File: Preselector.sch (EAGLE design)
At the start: 100 parts, among them IC58 LMZ31707RVQ, Q2 FDV303N, X1 0733660061, X2 0733660061, X3 0733660061, X4 0733660061, X5 0733660061, X6 0733660061

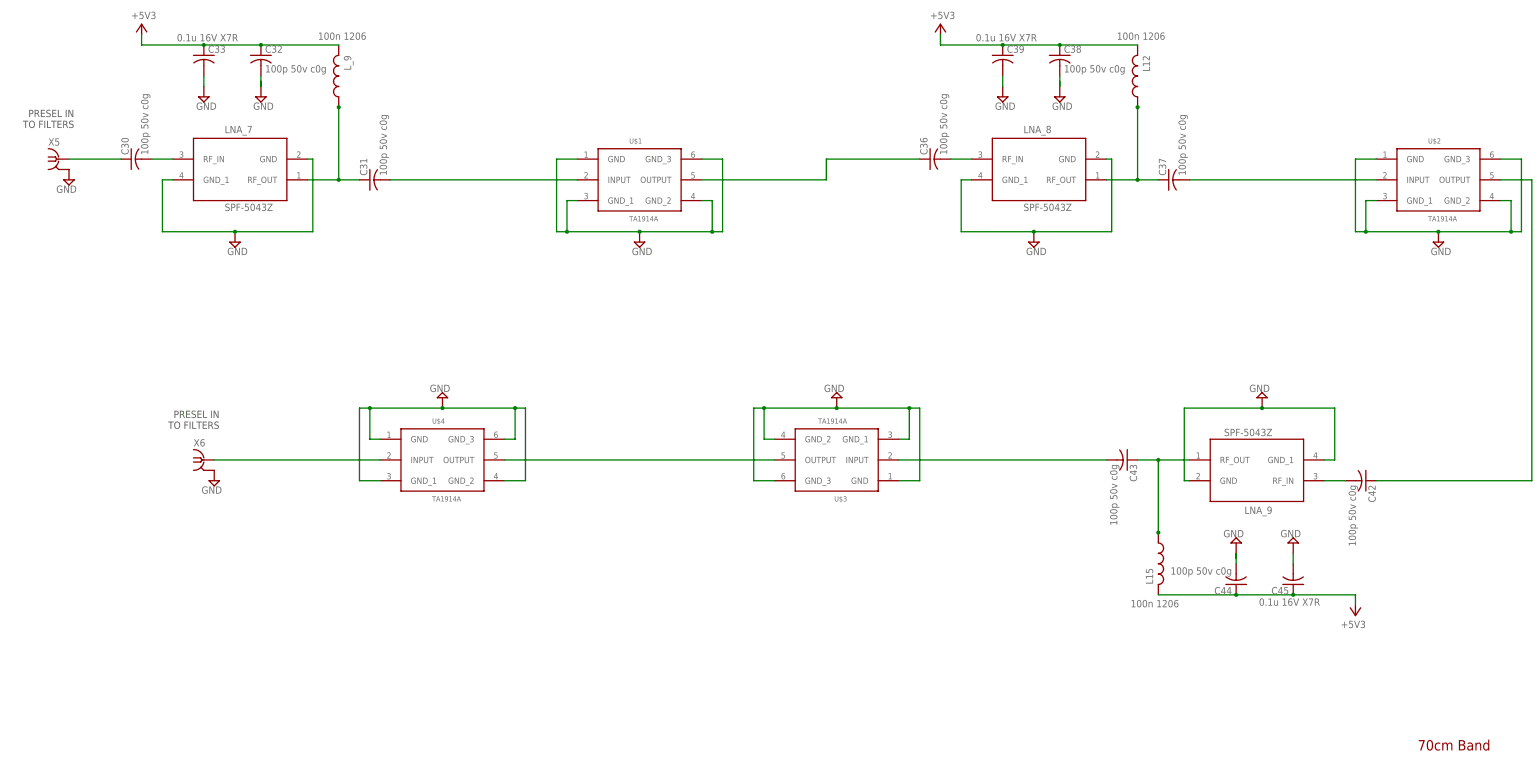
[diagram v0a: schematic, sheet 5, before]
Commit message: Ken, I renamed the capacitors and inductors in order as they appear on each Filter and LNA respectively. If you see anything wrong let me know.
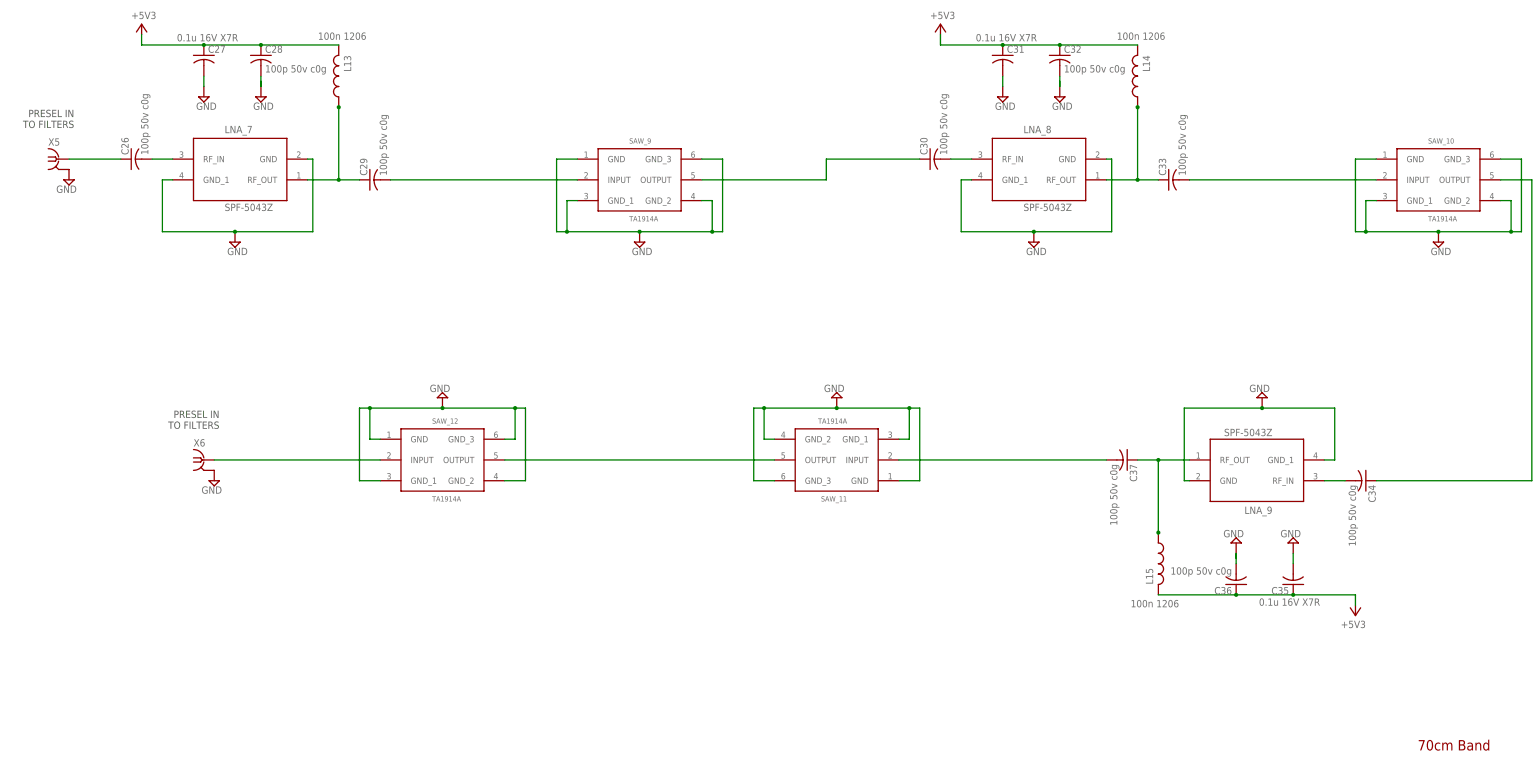
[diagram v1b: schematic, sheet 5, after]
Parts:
- removed C38, C43, C44: 100p 50v c0g, rcl:C-USC0603K
- removed C39: 0.1u 16V X7R, rcl:C-USC0603K
- removed L_8: 100n 1206, NewSDR:L-US1206
- added C14, C17, C20, C21: 100p 50v c0g, rcl:C-USC0603K
- added L14: 100n 1206, NewSDR:L-US1206
- C19, C23, C27, C31: value 100p 50v c0g -> 0.1u 16V X7R
- C25, C29, C33: value 0.1u 16V X7R -> 100p 50v c0g
- renumbered C42 to C34, C45 to C35, C_20 to C16, C_21 to C15, L_00 to L11, L_7 to L10, L_9 to L13, U$1 to SAW_9, U$2 to SAW_10, U$3 to SAW_11, U$4 to SAW_12
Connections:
- net +5V3: now also C19.1, C20.1, C23.1, C27.1, C31.1, C36.1, L14.2; no longer C25.1, C29.1, C33.1, C38.1, C39.1, C44.1, L12.2
- net 1.25M_RF_IN: now also C17.2; no longer C19.2
- net 1.25M_RF_IN1: now also C22.2; no longer C26.2
- net 1.25M_RF_IN3: now also C18.1, C18.2; no longer C22.1, C22.2
- net 1.25M_RF_IN_: now also C21.2; no longer C23.2
- net 1.25M_RF_IN_1: now also C25.2; no longer C27.2
- net 1.2M5_RF_IN4: now also C22.1; no longer C26.1
- net 2M_RF_IN2: now also C14.1, C14.2; no longer C18.1, C18.2
- net 2M_RF_IN4: now also C26.1, C26.2; no longer C30.1, C30.2
- net 2M_RF_IN6: now also C30.2; no longer C36.2
- net GND: now also C19.2, C20.2, C23.2, C27.2, C31.2, C36.2; no longer C25.2, C29.2, C33.2, C38.2, C39.2, C44.2
- net GND1: now also C21.1; no longer C23.1
- net GND2: now also C17.1; no longer C19.1
- net GND3: now also L12.1; no longer L_8.1
- net GND4: now also C29.1; no longer C31.1
- net GND5: now also C33.1, L14.1; no longer C37.1, L12.1
- net GND6: now also C37.1; no longer C43.1
- net N$13: now also C25.1, L12.2; no longer C27.1, L_8.2
- net N$15: now also C29.2; no longer C31.2
- net N$16: now also C30.1; no longer C36.1
- net N$17: now also C33.2; no longer C37.2
- net N$19: now also C37.2; no longer C43.2
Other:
- moved on the sheet: C18, C19, C22, C23, C24, C25, C30, C31, C32, C33, C36, C37

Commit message: Deleted .brd to sync schematic for annotation
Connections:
- removed net N$3: C8.2, L5.2, SAW_3.INPUT
- net 2M_RF_IN: now also C8.2, L5.2, SAW_3.INPUT
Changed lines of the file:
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@@
 <junction x="156.21" y="152.4"/>
+</segment>
+<segment>
+<pinref part="C8" gate="G$1" pin="2"/>
+<pinref part="SAW_3" gate="G$1" pin="INPUT"/>
+<wire x1="322.58" y1="224.79" x2="332.74" y2="224.79" width="0.1524" layer="91"/>
+<pinref part="L5" gate="G$1" pin="2"/>
+<wire x1="332.74" y1="224.79" x2="347.98" y2="224.79" width="0.1524" layer="91"/>
+<wire x1="332.74" y1="224.79" x2="332.74" y2="232.41" width="0.1524" layer="91"/>
+<junction x="332.74" y="224.79"/>
 </segment>
 </net>
@@
 </segment>
 </net>
-<net name="N$3" class="0">
-<segment>
-<pinref part="C8" gate="G$1" pin="2"/>
-<pinref part="SAW_3" gate="G$1" pin="INPUT"/>
-<wire x1="322.58" y1="224.79" x2="332.74" y2="224.79" width="0.1524" layer="91"/>
-<pinref part="L5" gate="G$1" pin="2"/>
-<wire x1="332.74" y1="224.79" x2="347.98" y2="224.79" width="0.1524" layer="91"/>
-<wire x1="332.74" y1="224.79" x2="332.74" y2="232.41" width="0.1524" layer="91"/>
-<junction x="332.74" y="224.79"/>
-</segment>
-</net>

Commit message: 1.25M band added to PCB design
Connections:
- removed net GND1: C21.1, L11.1, LNA_5.RF_OUT
- removed net GND2: C17.1, L10.1, LNA_4.RF_OUT
- net 1.25M_RF_IN: now also C17.1, C21.1, L10.1, L11.1, LNA_4.RF_OUT, LNA_5.RF_OUT
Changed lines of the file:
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@@
 <wire x1="114.3" y1="175.26" x2="152.4" y2="175.26" width="0.1524" layer="91"/>
+</segment>
+<segment>
+<pinref part="L10" gate="G$1" pin="1"/>
+<junction x="101.6" y="193.04"/>
+<pinref part="C17" gate="G$1" pin="1"/>
+<pinref part="LNA_4" gate="G$1" pin="RF_OUT"/>
+<wire x1="93.98" y1="175.26" x2="101.6" y2="175.26" width="0.1524" layer="91"/>
+<wire x1="101.6" y1="175.26" x2="106.68" y2="175.26" width="0.1524" layer="91"/>
+<wire x1="101.6" y1="193.04" x2="101.6" y2="175.26" width="0.1524" layer="91"/>
+<junction x="101.6" y="175.26"/>
+</segment>
+<segment>
+<pinref part="L11" gate="G$1" pin="1"/>
+<junction x="294.64" y="190.5"/>
+<pinref part="C21" gate="G$1" pin="1"/>
+<pinref part="LNA_5" gate="G$1" pin="RF_OUT"/>
+<wire x1="287.02" y1="172.72" x2="294.64" y2="172.72" width="0.1524" layer="91"/>
+<wire x1="294.64" y1="172.72" x2="299.72" y2="172.72" width="0.1524" layer="91"/>
+<wire x1="294.64" y1="190.5" x2="294.64" y2="172.72" width="0.1524" layer="91"/>
+<junction x="294.64" y="172.72"/>
 </segment>
 </net>
@@
 </segment>
 </net>
-<net name="GND1" class="1">
-<segment>
-<pinref part="L11" gate="G$1" pin="1"/>
-<junction x="294.64" y="190.5"/>
-<pinref part="C21" gate="G$1" pin="1"/>
-<pinref part="LNA_5" gate="G$1" pin="RF_OUT"/>
-<wire x1="287.02" y1="172.72" x2="294.64" y2="172.72" width="0.1524" layer="91"/>
-<wire x1="294.64" y1="172.72" x2="299.72" y2="172.72" width="0.1524" layer="91"/>
-<wire x1="294.64" y1="190.5" x2="294.64" y2="172.72" width="0.1524" layer="91"/>
-<junction x="294.64" y="172.72"/>
-</segment>
-</net>
-<net name="GND2" class="1">
-<segment>
-<pinref part="L10" gate="G$1" pin="1"/>
-<junction x="101.6" y="193.04"/>
-<pinref part="C17" gate="G$1" pin="1"/>
-<pinref part="LNA_4" gate="G$1" pin="RF_OUT"/>
-<wire x1="93.98" y1="175.26" x2="101.6" y2="175.26" width="0.1524" layer="91"/>
-<wire x1="101.6" y1="175.26" x2="106.68" y2="175.26" width="0.1524" layer="91"/>
-<wire x1="101.6" y1="193.04" x2="101.6" y2="175.26" width="0.1524" layer="91"/>
-<junction x="101.6" y="175.26"/>
-</segment>
-</net>

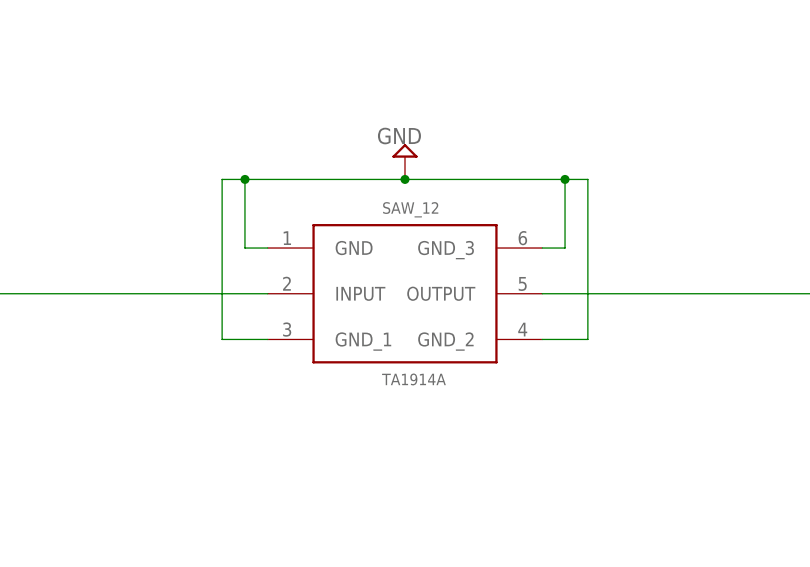
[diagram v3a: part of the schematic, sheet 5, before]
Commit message: kenneth, 70cm band is added to pcb
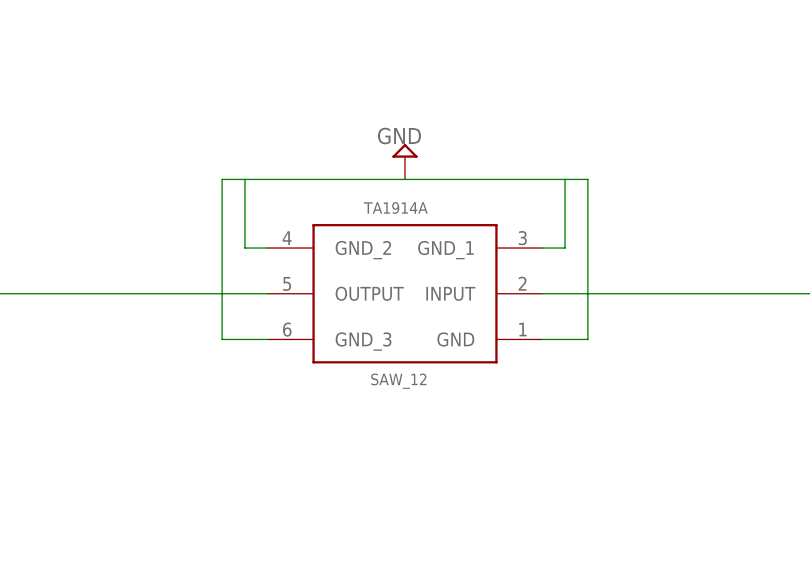
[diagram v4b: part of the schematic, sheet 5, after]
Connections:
- net GND4 renamed 70CM_RF_IN
- removed net N$21: SAW_12.INPUT, X6G$1.1
- new net N$56: SAW_12.OUTPUT, X6G$1.1
- net N$20: now also SAW_12.INPUT; no longer SAW_12.OUTPUT
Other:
- moved on the sheet: SAW_12
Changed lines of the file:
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@@
 </instance>
 <instance part="SAW_11" gate="G$1" x="220.98" y="99.06" rot="R180"/>
-<instance part="SAW_12" gate="G$1" x="124.46" y="99.06"/>
+<instance part="SAW_12" gate="G$1" x="124.46" y="99.06" rot="R180"/>
 <instance part="X6" gate="G$1" x="66.04" y="99.06" smashed="yes">
 <attribute name="NAME" x="63.5" y="102.362" size="1.778" layer="95"/>
@@
 </segment>
 <segment>
+<pinref part="SAW_12" gate="G$1" pin="GND"/>
 <wire x1="139.7" y1="93.98" x2="144.78" y2="93.98" width="0.1524" layer="91"/>
 <wire x1="144.78" y1="93.98" x2="144.78" y2="111.76" width="0.1524" layer="91"/>
 <pinref part="SUPPLY47" gate="GND" pin="GND"/>
 <wire x1="144.78" y1="111.76" x2="142.24" y2="111.76" width="0.1524" layer="91"/>
+<pinref part="SAW_12" gate="G$1" pin="GND_1"/>
 <wire x1="142.24" y1="111.76" x2="124.46" y2="111.76" width="0.1524" layer="91"/>
+<wire x1="139.7" y1="104.14" x2="142.24" y2="104.14" width="0.1524" layer="91"/>
+<wire x1="142.24" y1="104.14" x2="142.24" y2="111.76" width="0.1524" layer="91"/>
+<pinref part="SAW_12" gate="G$1" pin="GND_3"/>
 <wire x1="109.22" y1="93.98" x2="104.14" y2="93.98" width="0.1524" layer="91"/>
 <wire x1="104.14" y1="93.98" x2="104.14" y2="111.76" width="0.1524" layer="91"/>
 <wire x1="104.14" y1="111.76" x2="106.68" y2="111.76" width="0.1524" layer="91"/>
-<junction x="124.46" y="111.76"/>
+<pinref part="SAW_12" gate="G$1" pin="GND_2"/>
 <wire x1="106.68" y1="111.76" x2="124.46" y2="111.76" width="0.1524" layer="91"/>
 <wire x1="109.22" y1="104.14" x2="106.68" y2="104.14" width="0.1524" layer="91"/>
 <wire x1="106.68" y1="104.14" x2="106.68" y2="111.76" width="0.1524" layer="91"/>
-<junction x="106.68" y="111.76"/>
-<wire x1="139.7" y1="104.14" x2="142.24" y2="104.14" width="0.1524" layer="91"/>
-<wire x1="142.24" y1="104.14" x2="142.24" y2="111.76" width="0.1524" layer="91"/>
-<junction x="142.24" y="111.76"/>
-<pinref part="SAW_12" gate="G$1" pin="GND"/>
-<pinref part="SAW_12" gate="G$1" pin="GND_1"/>
-<pinref part="SAW_12" gate="G$1" pin="GND_2"/>
-<pinref part="SAW_12" gate="G$1" pin="GND_3"/>
 </segment>
 </net>
@@
 </segment>
 </net>
-<net name="GND4" class="1">
+<net name="70CM_RF_IN" class="1">
 <segment>
 <pinref part="L13" gate="G$1" pin="1"/>
@@
 <segment>
 <pinref part="SAW_11" gate="G$1" pin="OUTPUT"/>
+<pinref part="SAW_12" gate="G$1" pin="INPUT"/>
+<wire x1="205.74" y1="99.06" x2="139.7" y2="99.06" width="0.1524" layer="91"/>
+</segment>
+</net>
+<net name="N$56" class="0">
+<segment>
 <pinref part="SAW_12" gate="G$1" pin="OUTPUT"/>
-<wire x1="205.74" y1="99.06" x2="139.7" y2="99.06" width="0.1524" layer="91"/>
-</segment>
-</net>
-<net name="N$21" class="0">
-<segment>
-<pinref part="SAW_12" gate="G$1" pin="INPUT"/>
 <pinref part="X6" gate="G$1" pin="1"/>
 <wire x1="109.22" y1="99.06" x2="68.58" y2="99.06" width="0.1524" layer="91"/>

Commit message: Fixed s511215 device in library, added 4m to schematic and finished 4m on the board.
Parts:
- added C38, C42, C46, C50: 160p 50v c0g, rcl:C-USC0603K
- added C39, C43, C47, C51: 180p 50v c0g, rcl:C-USC0603K
- added C40, C44, C48: 0.1u 16V X7R, rcl:C-USC0603K
- added C41, C45, C49: 100p 50v c0g, rcl:C-USC0603K
- added FL1, FL2, FL3, FL4: S511214, SeniorDesign:S511214
- added L16, L17, L18, L19, L20, L21, L22, L23, L24, L25, L26: 100n 1206, NewSDR:L-US1206
- added LNA_10, LNA_11, LNA_12: SPF-5043Z, SeniorDesign:SPF-5043Z
- added X7, X8: 0733660061, con-coax:BU-SMA-V
- TP10: value TPSQTP20SQD -> TPSQB1,27; device testpad:TPSQTP20SQD -> testpad:TPSQB1,27
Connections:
- new net 4M_RF_IN: C38.1, C38.2, C39.1, C39.2, C42.1, C42.2, C43.2, C46.1, C46.2, C47.1, C47.2, C50.1, C50.2, C51.1, C51.2, FL1.INPUT, FL1.OUTPUT, FL2.INPUT, FL3.INPUT, FL3.OUTPUT, FL4.INPUT, FL4.OUTPUT, L16.1, L17.1, L18.1, L19.1, L20.1, L21.1, L22.1, L23.1, L24.1, L25.1, L26.1, LNA_10.RF_IN, LNA_10.RF_OUT, LNA_11.RF_IN, LNA_11.RF_OUT, LNA_12.RF_IN, LNA_12.RF_OUT, X7G$1.1, X8G$1.1
- new net 4M_RF_IN1: C43.1, FL2.OUTPUT
- net +5V3: now also C40.1, C41.1, C44.1, C45.1, C48.1, C49.1, L18.2, L21.2, L24.2
- net GND: now also C40.2, C41.2, C44.2, C45.2, C48.2, C49.2, FL1.GROUND_1, FL1.GROUND_2, FL1.GROUND_3, FL1.GROUND_4, FL1.GROUND_5, FL1.GROUND_6, FL1.INPUT_GROUND, FL1.OUTPUT_GROUND, FL2.GROUND_1, FL2.GROUND_2, FL2.GROUND_3, FL2.GROUND_4, FL2.GROUND_5, FL2.GROUND_6, FL2.INPUT_GROUND, FL2.OUTPUT_GROUND, FL3.GROUND_1, FL3.GROUND_2, FL3.GROUND_3, FL3.GROUND_4, FL3.GROUND_5, FL3.GROUND_6, FL3.INPUT_GROUND, FL3.OUTPUT_GROUND, FL4.GROUND_1, FL4.GROUND_2, FL4.GROUND_3, FL4.GROUND_4, FL4.GROUND_5, FL4.GROUND_6, FL4.INPUT_GROUND, FL4.OUTPUT_GROUND, L16.2, L17.2, L19.2, L20.2, L22.2, L23.2, L25.2, L26.2, LNA_10.GND, LNA_10.GND_1, LNA_11.GND, LNA_11.GND_1, LNA_12.GND, LNA_12.GND_1, X7G$1.GND, X8G$1.GND
